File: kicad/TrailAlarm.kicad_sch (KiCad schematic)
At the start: 33 parts, among them IC1 MAX865EUA+T, J1 Conn_01x03, J2 Conn_01x01_Male, J3 Adafruit ADS1115, J4 Bat, Q1 2N3904, SW1 SW_DIP_x01, U1 TLC274, U2 TL074, U3 PocketBeagle

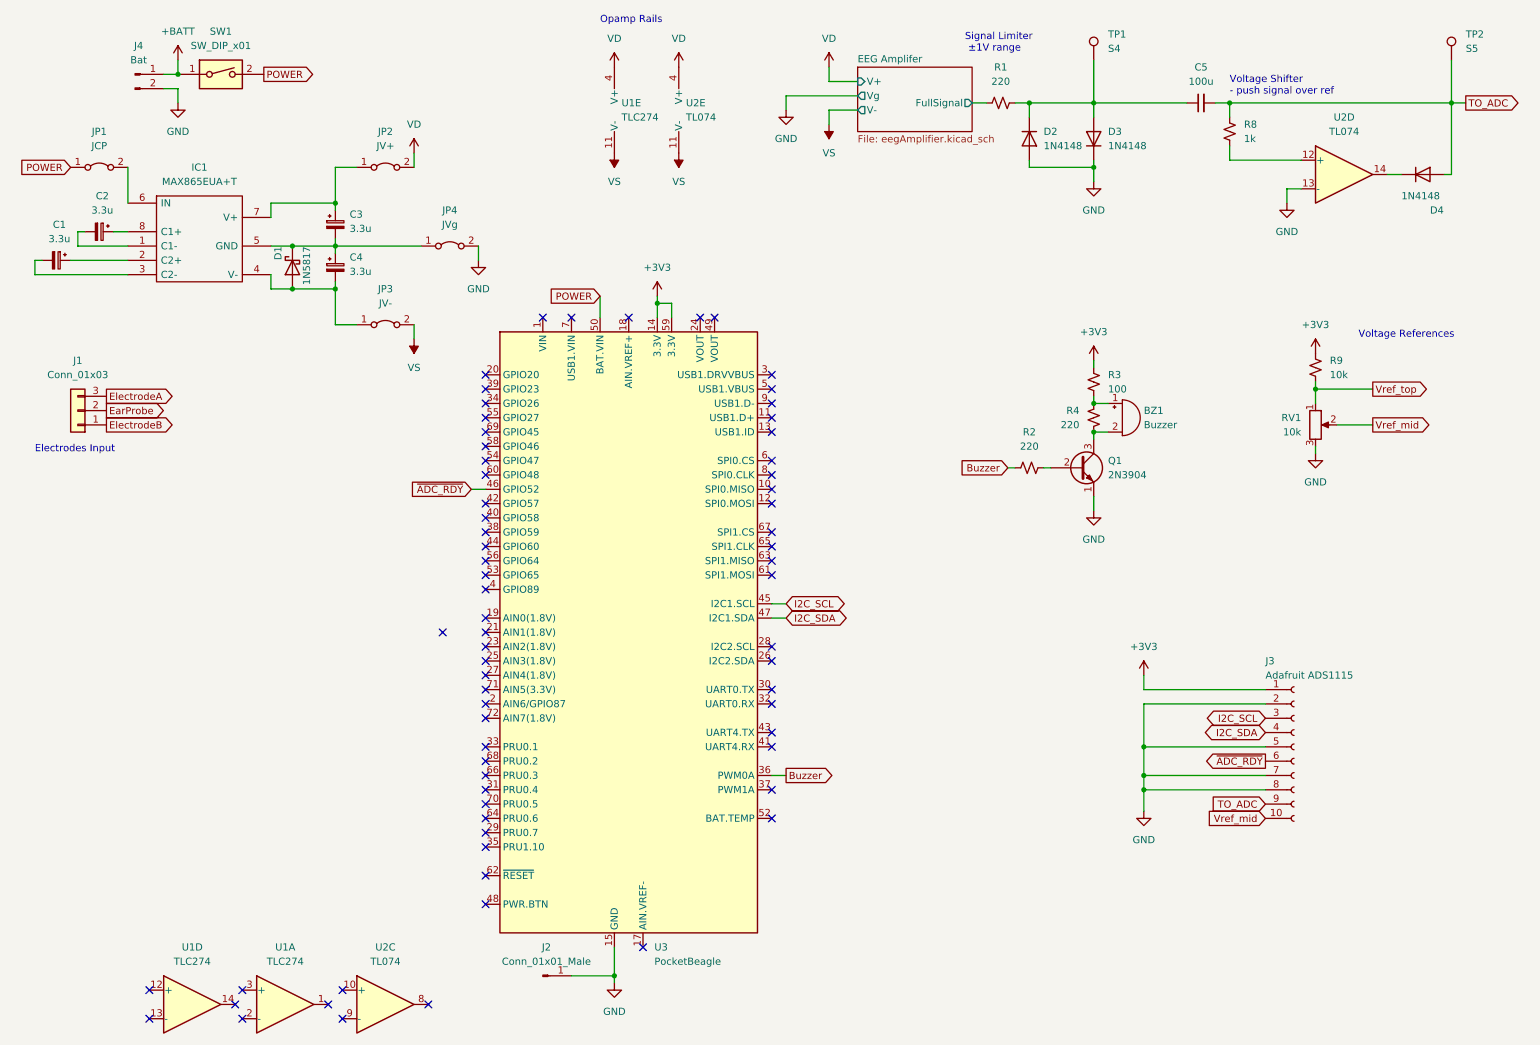
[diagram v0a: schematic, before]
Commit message: Updated schematic labels, PocketBeagle to separate sheet
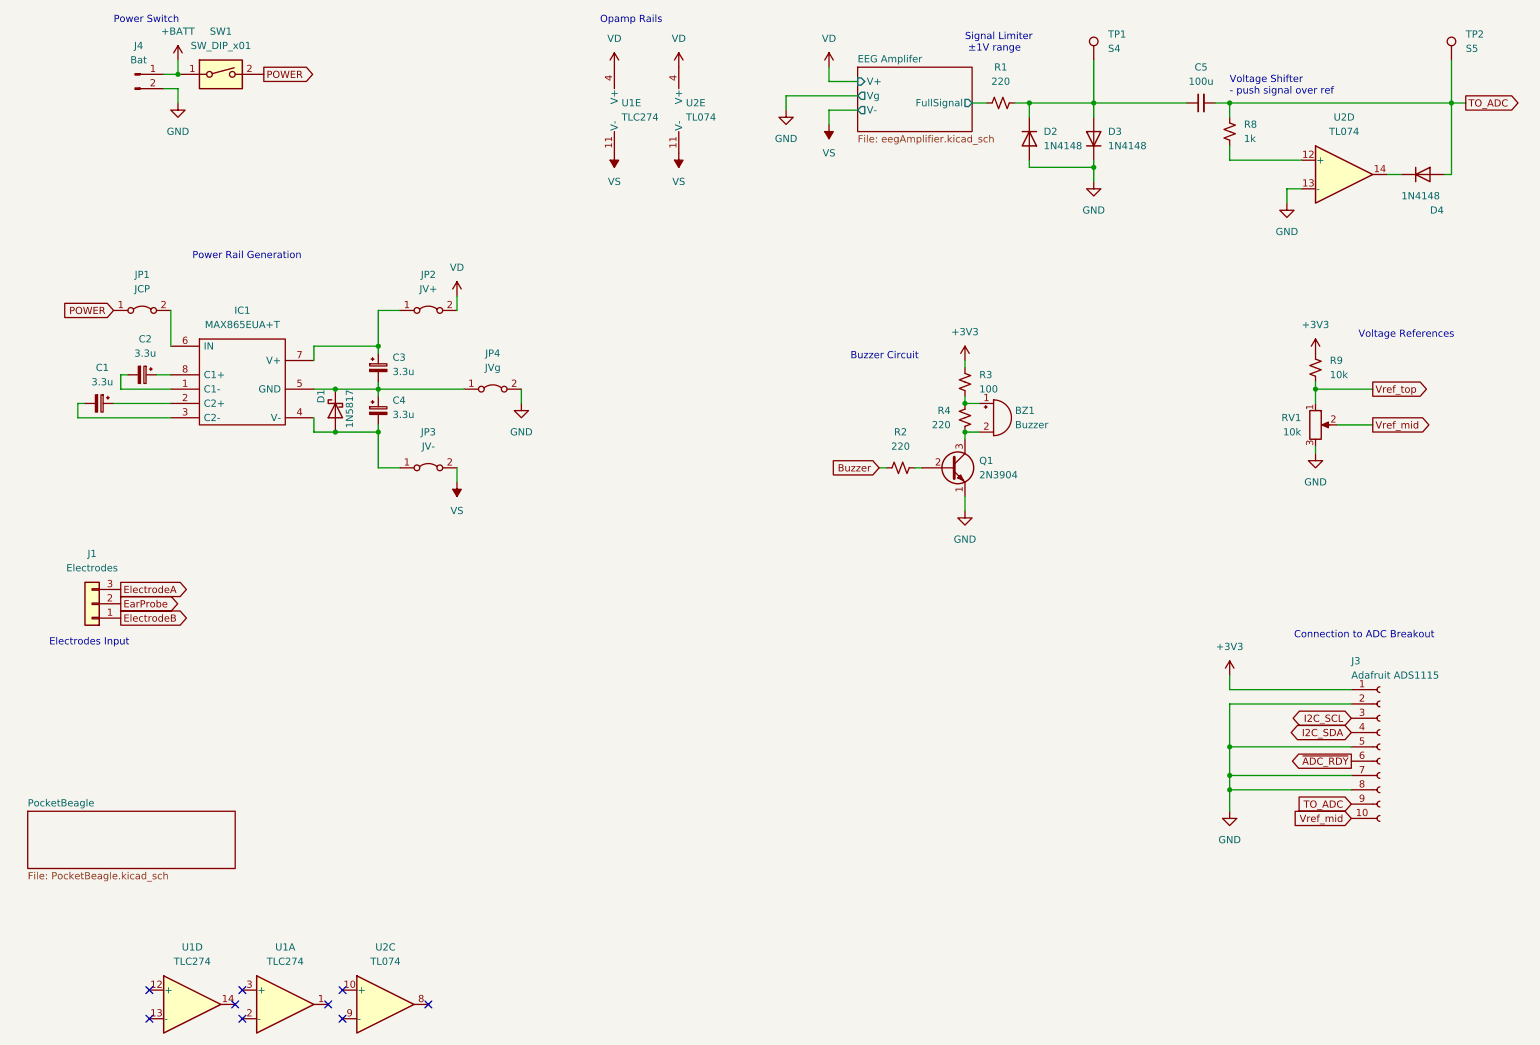
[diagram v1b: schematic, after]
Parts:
- removed J2: Conn_01x01_Male, Connector_PinHeader_2.54mm:PinHeader_1x01_P2.54mm_Vertical, symbol Connector:Conn_01x01_Male
- removed U3: PocketBeagle, Module:BeagleBoard_PocketBeagle, symbol MCU_Module:PocketBeagle
- J1: value Conn_01x03 -> Electrodes
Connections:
- no-connect marks 70 -> 9
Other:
- added sheet PocketBeagle (PocketBeagle.kicad_sch)
- note added: "Buzzer Circuit"
- note added: "Connection to ADC Breakout"
- note added: "Power Rail Generation"
- note added: "Power Switch"
- moved on the sheet: BZ1, C1, C2, C3, C4, D1, IC1, J1, J3, JP1, JP2, JP3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

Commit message: Updated layout
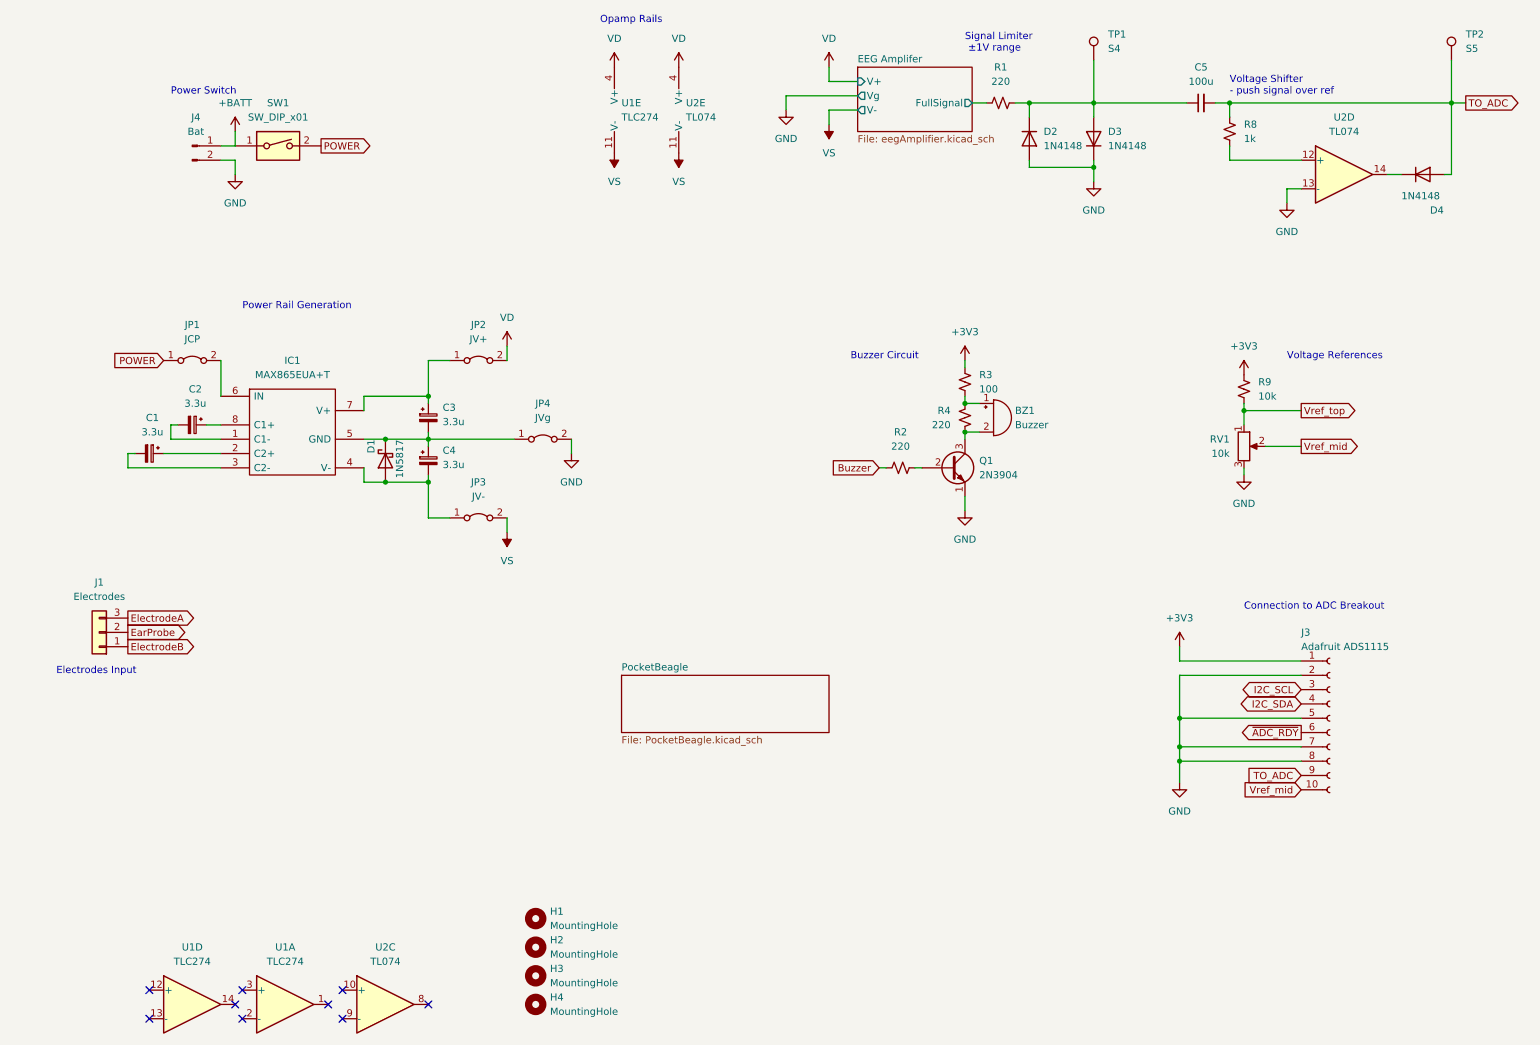
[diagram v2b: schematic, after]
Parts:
- added H1, H2, H3, H4: MountingHole, MountingHole:MountingHole_2.2mm_M2, symbol Mechanical:MountingHole
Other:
- moved on the sheet: C1, C2, C3, C4, D1, IC1, J1, J3, J4, JP1, JP2, JP3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
